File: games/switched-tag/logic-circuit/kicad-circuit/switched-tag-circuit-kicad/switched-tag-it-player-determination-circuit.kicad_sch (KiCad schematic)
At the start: 0 parts

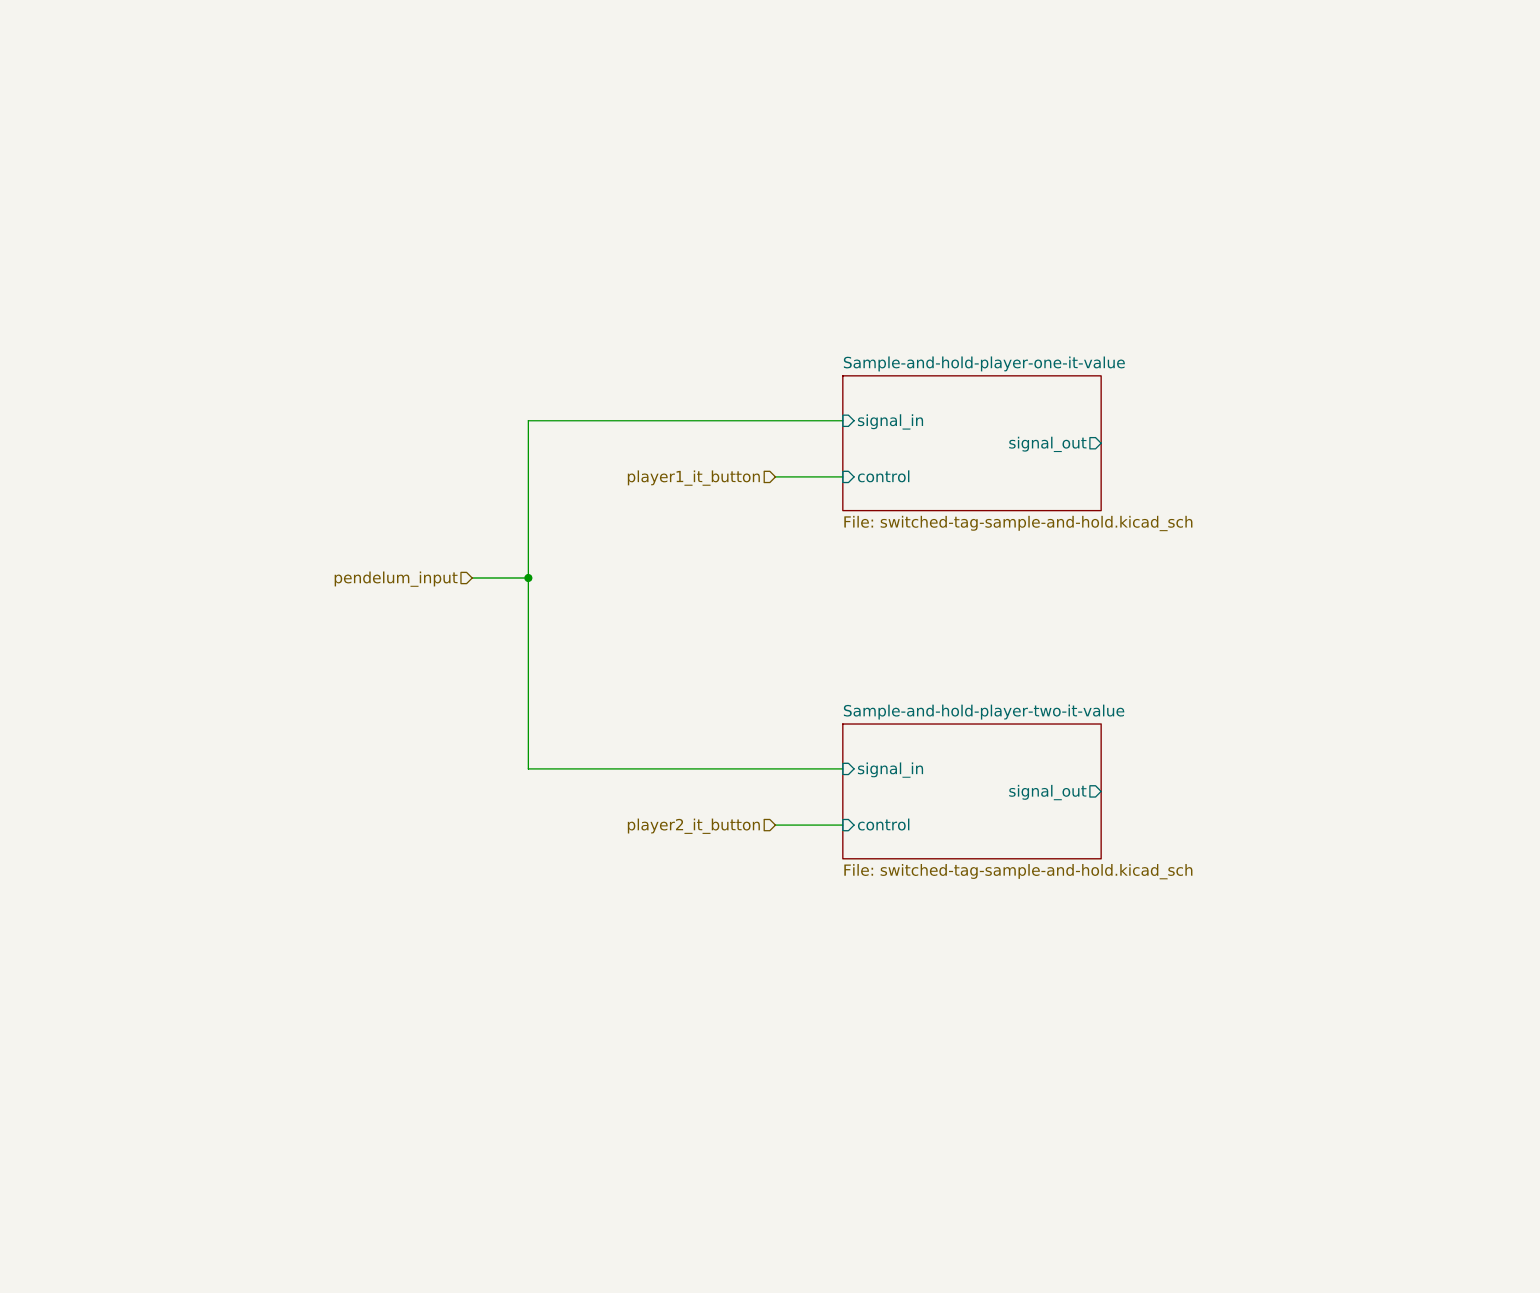
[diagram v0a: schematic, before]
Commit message: Saving progress on kicad schematic. Trying to set up ngspice simulation.
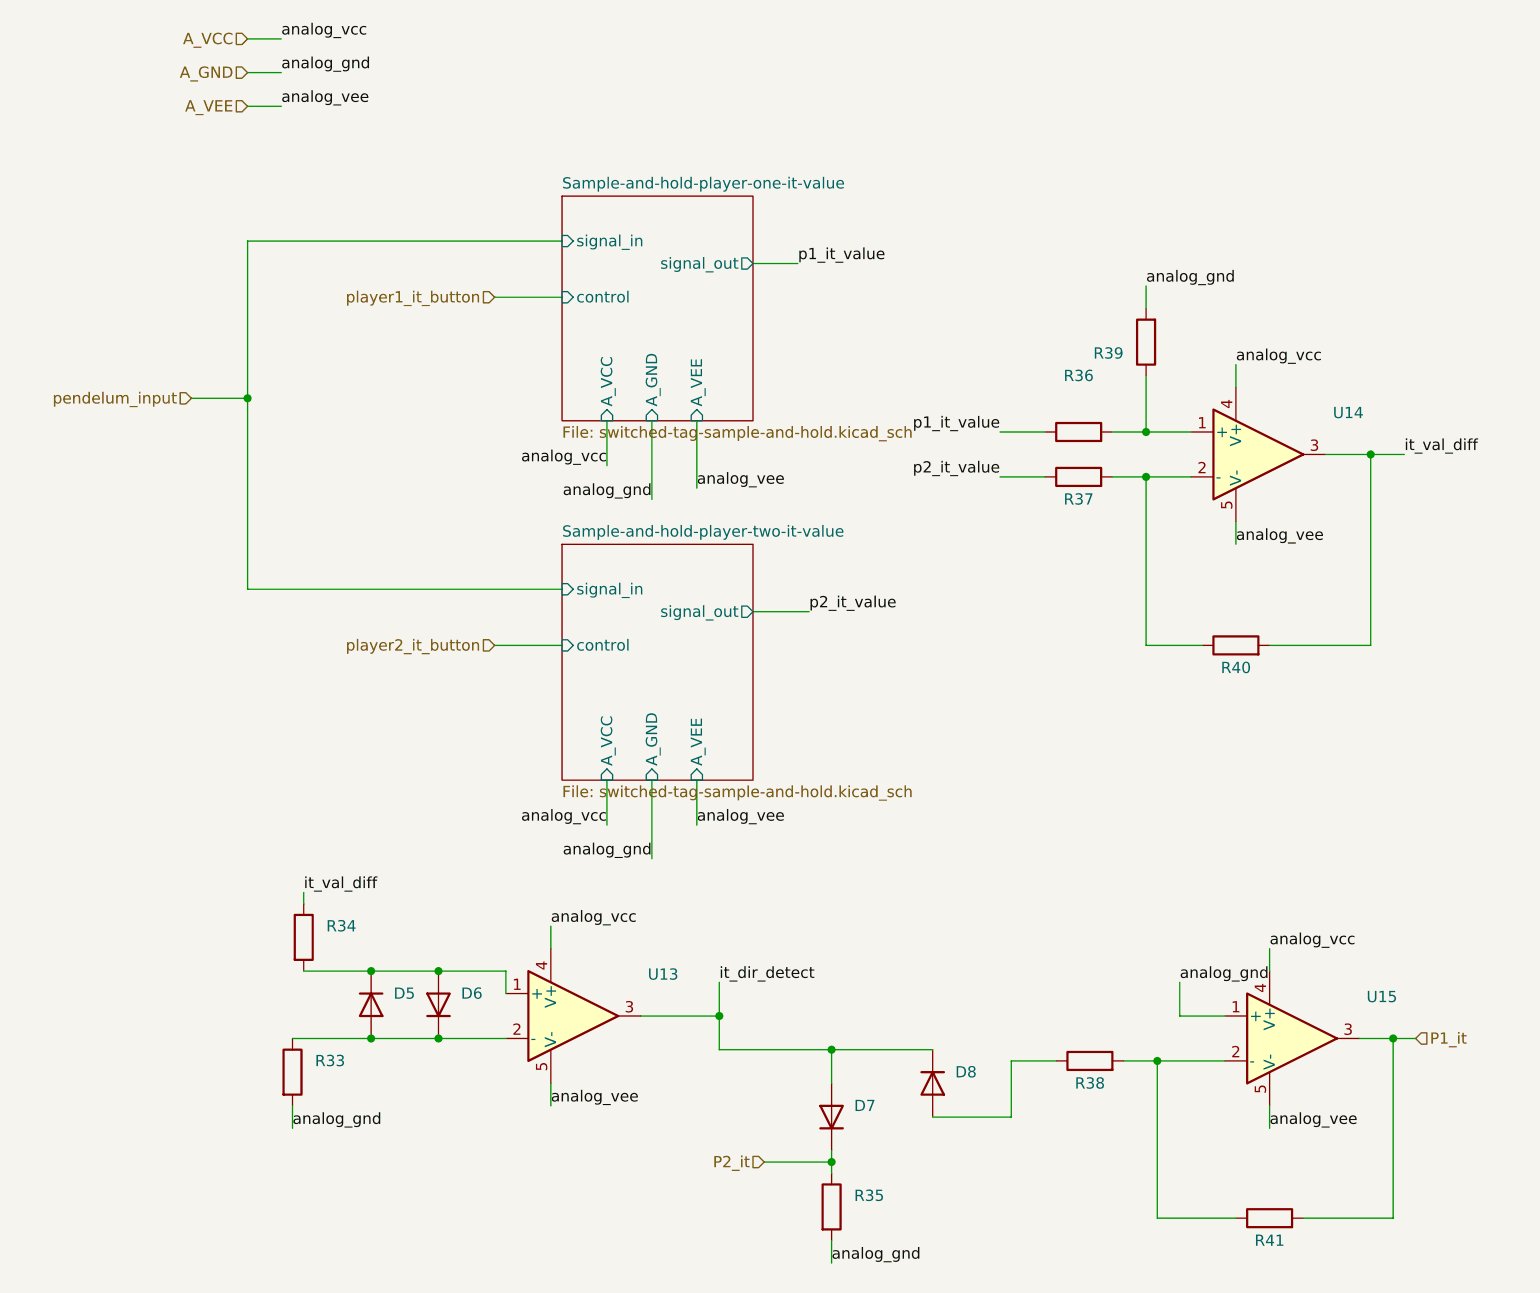
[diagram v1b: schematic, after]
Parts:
- added D5, D6, D7, D8: (no value), symbol Device:D
- added R33, R34, R35, R36, R37, R38, R39, R40, R41: (no value), symbol Device:R
- added U13, U14, U15: (no value), symbol Simulation_SPICE:OPAMP
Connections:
- new net: D5.1 (K), D6.2 (A), R34.2, U13.1 (+)
- new net: D5.2 (A), D6.1 (K), R33.1, U13.2 (-)
- new net: R36.2, R39.1, U14.1 (+)
- new net: D8.2 (A), R38.1
- new net: R38.2, R41.1, U15.2 (-)
- new net: R37.2, R40.1, U14.2 (-)
- new net A_GND: R33.2, R35.2, R39.2, U15.1 (+)
- new net A_VCC: U13.4 (V+), U14.4 (V+), U15.4 (V+)
- new net A_VEE: U13.5 (V-), U14.5 (V-), U15.5 (V-)
- new net P1_it: R41.2, U15.3
- new net P2_it: D7.1 (K), R35.1
- new net it_dir_detect: D7.2 (A), D8.1 (K), U13.3
- new net it_val_diff: R34.1, R40.2, U14.3
- new net p1_it_value: R36.1
- new net p2_it_value: R37.1
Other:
- sheet Sample-and-hold-player-one-it-value ports: added A_GND, A_VCC, A_VEE; removed none
- sheet Sample-and-hold-player-two-it-value ports: added A_GND, A_VCC, A_VEE; removed none

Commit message: Fixed problems with kicad circuit adn spice setup.
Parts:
- D5, D6, D7, D8: Spice_Model (none) -> D1N914; Spice_Netlist_Enabled (none) -> Y; Spice_Node_Sequence (none) -> 2 1; Spice_Primitive (none) -> D
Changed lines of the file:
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@@
+      (effects (font (size 1.27 1.27)) hide)
+    )
+    (property "Spice_Model" "D1N914" (id 5) (at 115.57 152.4 0)
+      (effects (font (size 1.27 1.27)) hide)
+    )
+    (property "Spice_Netlist_Enabled" "Y" (id 6) (at 115.57 152.4 0)
+      (effects (font (size 1.27 1.27)) hide)
+    )
+    (property "Spice_Primitive" "D" (id 7) (at 115.57 152.4 0)
+      (effects (font (size 1.27 1.27)) hide)
+    )
+    (property "Spice_Node_Sequence" "2 1" (id 8) (at 115.57 152.4 0)
       (effects (font (size 1.27 1.27)) hide)
     )
@@
     )
     (property "Spice_Lib_File" "/home/pab/Inventions/analog-circuit-game-console/ms-circuit-video-games/spice-models/1N914.lib" (id 4) (at 104.14 156.21 0)
+      (effects (font (size 1.27 1.27)) hide)
+    )
+    (property "Spice_Model" "D1N914" (id 5) (at 104.14 156.21 0)
+      (effects (font (size 1.27 1.27)) hide)
+    )
+    (property "Spice_Netlist_Enabled" "Y" (id 6) (at 104.14 156.21 0)
+      (effects (font (size 1.27 1.27)) hide)
+    )
+    (property "Spice_Primitive" "D" (id 7) (at 104.14 156.21 0)
+      (effects (font (size 1.27 1.27)) hide)
+    )
+    (property "Spice_Node_Sequence" "2 1" (id 8) (at 104.14 156.21 0)
       (effects (font (size 1.27 1.27)) hide)
     )
@@
     )
     (property "Spice_Lib_File" "/home/pab/Inventions/analog-circuit-game-console/ms-circuit-video-games/spice-models/1N914.lib" (id 4) (at 52.07 143.51 0)
+      (effects (font (size 1.27 1.27)) hide)
+    )
+    (property "Spice_Model" "D1N914" (id 5) (at 52.07 143.51 0)
+      (effects (font (size 1.27 1.27)) hide)
+    )
+    (property "Spice_Netlist_Enabled" "Y" (id 6) (at 52.07 143.51 0)
+      (effects (font (size 1.27 1.27)) hide)
+    )
+    (property "Spice_Primitive" "D" (id 7) (at 52.07 143.51 0)
+      (effects (font (size 1.27 1.27)) hide)
+    )
+    (property "Spice_Node_Sequence" "2 1" (id 8) (at 52.07 143.51 0)
       (effects (font (size 1.27 1.27)) hide)
     )
@@
       (effects (font (size 1.27 1.27)) hide)
     )
+    (property "Spice_Model" "D1N914" (id 5) (at 59.69 143.51 0)
+      (effects (font (size 1.27 1.27)) hide)
+    )
+    (property "Spice_Netlist_Enabled" "Y" (id 6) (at 59.69 143.51 0)
+      (effects (font (size 1.27 1.27)) hide)
+    )
+    (property "Spice_Primitive" "D" (id 7) (at 59.69 143.51 0)
+      (effects (font (size 1.27 1.27)) hide)
+    )
+    (property "Spice_Node_Sequence" "2 1" (id 8) (at 59.69 143.51 0)
+      (effects (font (size 1.27 1.27)) hide)
+    )
